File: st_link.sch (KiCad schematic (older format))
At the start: 29 parts

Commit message: STM32 schematic mostly done
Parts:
- Y?: value Crystal -> 8M
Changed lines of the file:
@@
 $Descr A4 11693 8268
 encoding utf-8
-Sheet 2 2
+Sheet 2 3
 Title "STM32 devboard with .05\" headers"
 Date ""
@@
 P 3700 2800
 AR Path="/5DFA8BC2" Ref="#PWR?"  Part="1"
-AR Path="/5DF7E971/5DFA8BC2" Ref="#PWR?"  Part="1"
-F 0 "#PWR?" H 3700 2650 50  0001 C CNN
+AR Path="/5DF7E971/5DFA8BC2" Ref="#PWR0101"  Part="1"
+F 0 "#PWR0101" H 3700 2650 50  0001 C CNN
 F 1 "+3V3" H 3715 2973 50  0000 C CNN
 F 2 "" H 3700 2800 50  0001 C CNN
@@
 P 3650 6200
 AR Path="/5DFA8BD5" Ref="#PWR?"  Part="1"
-AR Path="/5DF7E971/5DFA8BD5" Ref="#PWR?"  Part="1"
-F 0 "#PWR?" H 3650 5950 50  0001 C CNN
+AR Path="/5DF7E971/5DFA8BD5" Ref="#PWR0102"  Part="1"
+F 0 "#PWR0102" H 3650 5950 50  0001 C CNN
 F 1 "GND" H 3655 6027 50  0000 C CNN
 F 2 "" H 3650 6200 50  0001 C CNN
@@
 $EndComp
 $Comp
-L power:+3V3 #PWR?
+L power:+3V3 #PWR0103
 U 1 1 5DFA8BFA
 P 2400 2800
-F 0 "#PWR?" H 2400 2650 50  0001 C CNN
+F 0 "#PWR0103" H 2400 2650 50  0001 C CNN
 F 1 "+3V3" H 2415 2973 50  0000 C CNN
 F 2 "" H 2400 2800 50  0001 C CNN
@@
 P 2500 4000
 AR Path="/5DFA8C00" Ref="#PWR?"  Part="1"
-AR Path="/5DF7E971/5DFA8C00" Ref="#PWR?"  Part="1"
-F 0 "#PWR?" H 2500 3750 50  0001 C CNN
+AR Path="/5DF7E971/5DFA8C00" Ref="#PWR0104"  Part="1"
+F 0 "#PWR0104" H 2500 3750 50  0001 C CNN
 F 1 "GND" H 2505 3827 50  0000 C CNN
 F 2 "" H 2500 4000 50  0001 C CNN
@@
 P 1800 3900
 F 0 "Y?" H 1800 4168 50  0000 C CNN
-F 1 "Crystal" H 1800 4077 50  0000 C CNN
+F 1 "8M" H 1800 4077 50  0000 C CNN
 F 2 "" H 1800 3900 50  0001 C CNN
 F 3 "~" H 1800 3900 50  0001 C CNN
@@
 Connection ~ 2050 3900
 $Comp
-L power:GND #PWR?
+L power:GND #PWR0105
 U 1 1 5DFA8C35
 P 2050 4300
-F 0 "#PWR?" H 2050 4050 50  0001 C CNN
+F 0 "#PWR0105" H 2050 4050 50  0001 C CNN
 F 1 "GND" H 2055 4127 50  0000 C CNN
 F 2 "" H 2050 4300 50  0001 C CNN
@@
 $EndComp
 $Comp
-L power:GND #PWR?
+L power:GND #PWR0106
 U 1 1 5DFA8C3B
 P 1550 4300
-F 0 "#PWR?" H 1550 4050 50  0001 C CNN
+F 0 "#PWR0106" H 1550 4050 50  0001 C CNN
 F 1 "GND" H 1555 4127 50  0000 C CNN
 F 2 "" H 1550 4300 50  0001 C CNN
@@
 	2050 4200 2050 4300
 $Comp
-L power:GND #PWR?
+L power:GND #PWR0107
 U 1 1 5DFA8C43
 P 2900 5900
-F 0 "#PWR?" H 2900 5650 50  0001 C CNN
+F 0 "#PWR0107" H 2900 5650 50  0001 C CNN
 F 1 "GND" H 2905 5727 50  0000 C CNN
 F 2 "" H 2900 5900 50  0001 C CNN
@@
 P 5050 5750
 AR Path="/5DFA8C9C" Ref="#PWR?"  Part="1"
-AR Path="/5DF7E971/5DFA8C9C" Ref="#PWR?"  Part="1"
-F 0 "#PWR?" H 5050 5500 50  0001 C CNN
+AR Path="/5DF7E971/5DFA8C9C" Ref="#PWR0108"  Part="1"
+F 0 "#PWR0108" H 5050 5500 50  0001 C CNN
 F 1 "GND" H 5055 5577 50  0000 C CNN
 F 2 "" H 5050 5750 50  0001 C CNN
@@
 P 8550 2400
 AR Path="/5DFA8CA2" Ref="#PWR?"  Part="1"
-AR Path="/5DF7E971/5DFA8CA2" Ref="#PWR?"  Part="1"
-F 0 "#PWR?" H 8550 2250 50  0001 C CNN
+AR Path="/5DF7E971/5DFA8CA2" Ref="#PWR0109"  Part="1"
+F 0 "#PWR0109" H 8550 2250 50  0001 C CNN
 F 1 "+3V3" H 8565 2573 50  0000 C CNN
 F 2 "" H 8550 2400 50  0001 C CNN
@@
 P 9000 3150
 AR Path="/5DFA8CCF" Ref="#PWR?"  Part="1"
-AR Path="/5DF7E971/5DFA8CCF" Ref="#PWR?"  Part="1"
-F 0 "#PWR?" H 9000 2900 50  0001 C CNN
+AR Path="/5DF7E971/5DFA8CCF" Ref="#PWR0110"  Part="1"
+F 0 "#PWR0110" H 9000 2900 50  0001 C CNN
 F 1 "GND" H 9005 2977 50  0000 C CNN
 F 2 "" H 9000 3150 50  0001 C CNN
@@
 P 10150 4400
 AR Path="/5DFA8CD8" Ref="#PWR?"  Part="1"
-AR Path="/5DF7E971/5DFA8CD8" Ref="#PWR?"  Part="1"
-F 0 "#PWR?" H 10150 4150 50  0001 C CNN
+AR Path="/5DF7E971/5DFA8CD8" Ref="#PWR0111"  Part="1"
+F 0 "#PWR0111" H 10150 4150 50  0001 C CNN
 F 1 "GND" H 10155 4227 50  0000 C CNN
 F 2 "" H 10150 4400 50  0001 C CNN
@@
 P 5050 4650
 AR Path="/5DFA8CF6" Ref="#PWR?"  Part="1"
-AR Path="/5DF7E971/5DFA8CF6" Ref="#PWR?"  Part="1"
-F 0 "#PWR?" H 5050 4500 50  0001 C CNN
+AR Path="/5DF7E971/5DFA8CF6" Ref="#PWR0112"  Part="1"
+F 0 "#PWR0112" H 5050 4500 50  0001 C CNN
 F 1 "+3V3" H 5065 4823 50  0000 C CNN
 F 2 "" H 5050 4650 50  0001 C CNN
@@
 P 9300 2700
 AR Path="/5DFA8D0C" Ref="#PWR?"  Part="1"
-AR Path="/5DF7E971/5DFA8D0C" Ref="#PWR?"  Part="1"
-F 0 "#PWR?" H 9300 2550 50  0001 C CNN
+AR Path="/5DF7E971/5DFA8D0C" Ref="#PWR0113"  Part="1"
+F 0 "#PWR0113" H 9300 2550 50  0001 C CNN
 F 1 "+5V" H 9315 2873 50  0000 C CNN
 F 2 "" H 9300 2700 50  0001 C CNN
@@
 P 9350 1450
 AR Path="/5DFA8D3E" Ref="#PWR?"  Part="1"
-AR Path="/5DF7E971/5DFA8D3E" Ref="#PWR?"  Part="1"
-F 0 "#PWR?" H 9350 1300 50  0001 C CNN
+AR Path="/5DF7E971/5DFA8D3E" Ref="#PWR0114"  Part="1"
+F 0 "#PWR0114" H 9350 1300 50  0001 C CNN
 F 1 "+3V3" H 9365 1623 50  0000 C CNN
 F 2 "" H 9350 1450 50  0001 C CNN
@@
 P 9350 1850
 AR Path="/5DFA8D44" Ref="#PWR?"  Part="1"
-AR Path="/5DF7E971/5DFA8D44" Ref="#PWR?"  Part="1"
-F 0 "#PWR?" H 9350 1600 50  0001 C CNN
+AR Path="/5DF7E971/5DFA8D44" Ref="#PWR0115"  Part="1"
+F 0 "#PWR0115" H 9350 1600 50  0001 C CNN
 F 1 "GND" H 9355 1677 50  0000 C CNN
 F 2 "" H 9350 1850 50  0001 C CNN
@@
 P 2000 3300
 AR Path="/5DFA8D5B" Ref="#PWR?"  Part="1"
-AR Path="/5DF7E971/5DFA8D5B" Ref="#PWR?"  Part="1"
-F 0 "#PWR?" H 2000 3050 50  0001 C CNN
+AR Path="/5DF7E971/5DFA8D5B" Ref="#PWR0116"  Part="1"
+F 0 "#PWR0116" H 2000 3050 50  0001 C CNN
 F 1 "GND" H 2005 3127 50  0000 C CNN
 F 2 "" H 2000 3300 50  0001 C CNN
@@
 P 9650 5700
 AR Path="/5DFA8D65" Ref="#PWR?"  Part="1"
-AR Path="/5DF7E971/5DFA8D65" Ref="#PWR?"  Part="1"
-F 0 "#PWR?" H 9650 5450 50  0001 C CNN
+AR Path="/5DF7E971/5DFA8D65" Ref="#PWR0117"  Part="1"
+F 0 "#PWR0117" H 9650 5450 50  0001 C CNN
 F 1 "GND" H 9655 5527 50  0000 C CNN
 F 2 "" H 9650 5700 50  0001 C CNN
@@
 P 9650 5100
 AR Path="/5DFA8D6D" Ref="#PWR?"  Part="1"
-AR Path="/5DF7E971/5DFA8D6D" Ref="#PWR?"  Part="1"
-F 0 "#PWR?" H 9650 4950 50  0001 C CNN
+AR Path="/5DF7E971/5DFA8D6D" Ref="#PWR0118"  Part="1"
+F 0 "#PWR0118" H 9650 4950 50  0001 C CNN
 F 1 "+3V3" H 9665 5273 50  0000 C CNN
 F 2 "" H 9650 5100 50  0001 C CNN
@@
 P 6250 2700
 AR Path="/5DFA8DB0" Ref="#PWR?"  Part="1"
-AR Path="/5DF7E971/5DFA8DB0" Ref="#PWR?"  Part="1"
-F 0 "#PWR?" H 6250 2450 50  0001 C CNN
+AR Path="/5DF7E971/5DFA8DB0" Ref="#PWR0119"  Part="1"
+F 0 "#PWR0119" H 6250 2450 50  0001 C CNN
 F 1 "GND" H 6255 2527 50  0000 C CNN
 F 2 "" H 6250 2700 50  0001 C CNN
@@
 P 7050 2000
 AR Path="/5DFA8DBB" Ref="#PWR?"  Part="1"
-AR Path="/5DF7E971/5DFA8DBB" Ref="#PWR?"  Part="1"
-F 0 "#PWR?" H 7050 1850 50  0001 C CNN
+AR Path="/5DF7E971/5DFA8DBB" Ref="#PWR0120"  Part="1"
+F 0 "#PWR0120" H 7050 1850 50  0001 C CNN
 F 1 "+3V3" H 7065 2173 50  0000 C CNN
 F 2 "" H 7050 2000 50  0001 C CNN
@@
 P 5450 2000
 AR Path="/5DFA8DC1" Ref="#PWR?"  Part="1"
-AR Path="/5DF7E971/5DFA8DC1" Ref="#PWR?"  Part="1"
-F 0 "#PWR?" H 5450 1850 50  0001 C CNN
+AR Path="/5DF7E971/5DFA8DC1" Ref="#PWR0121"  Part="1"
+F 0 "#PWR0121" H 5450 1850 50  0001 C CNN
 F 1 "+5V" H 5465 2173 50  0000 C CNN
 F 2 "" H 5450 2000 50  0001 C CNN

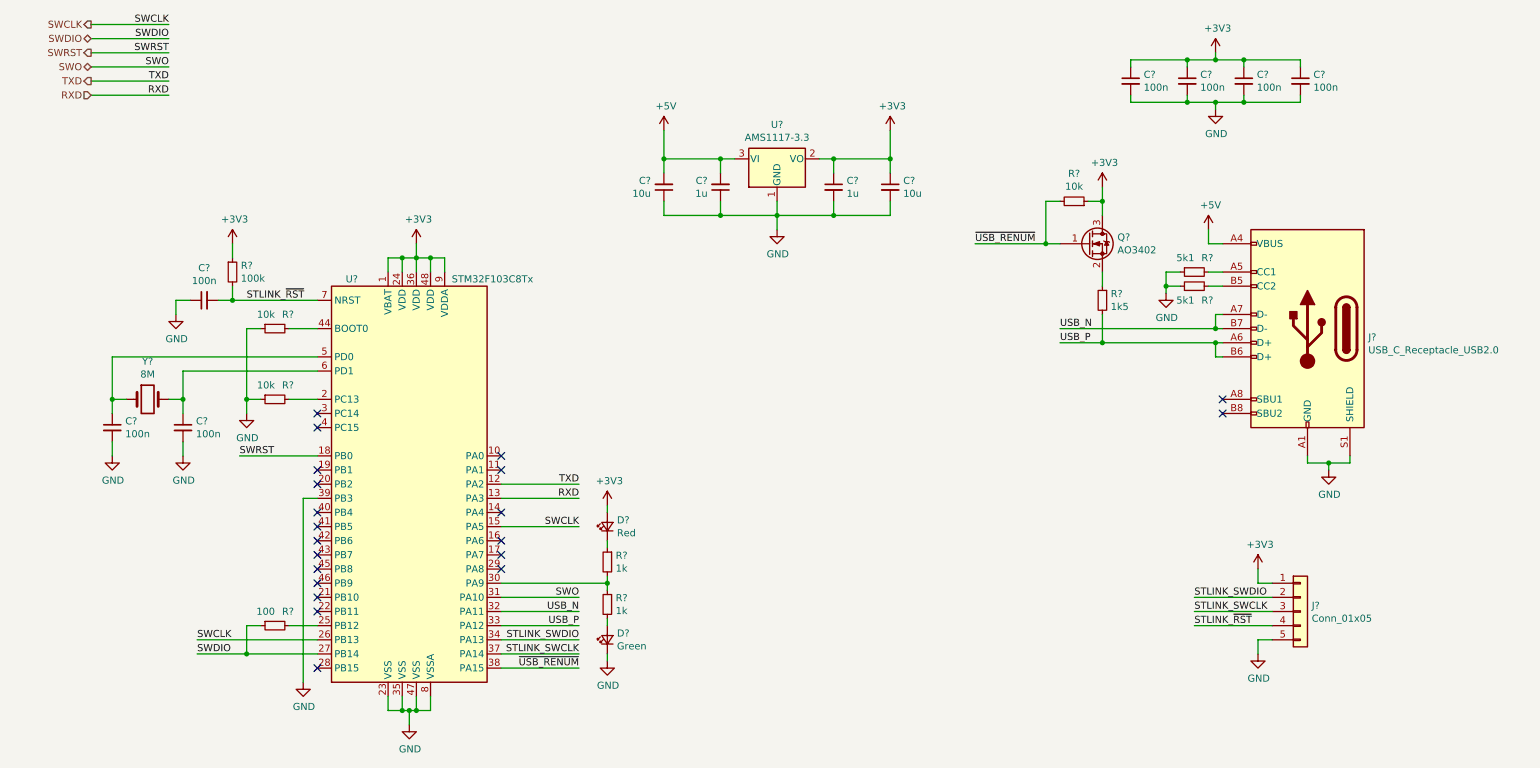
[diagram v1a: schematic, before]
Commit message: Better sch segmentation and add TCA6424A symbol
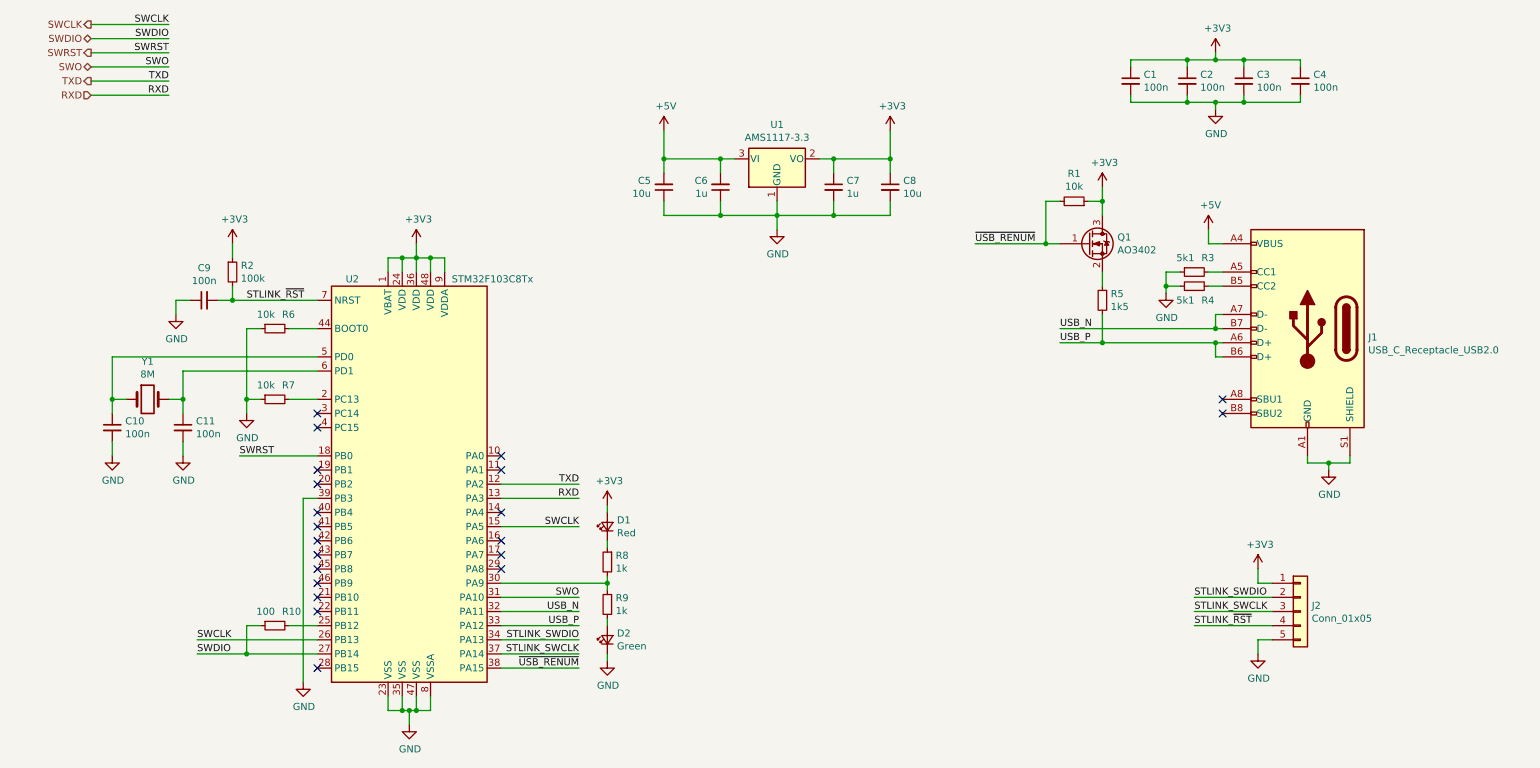
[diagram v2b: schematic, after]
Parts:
- C1, C10, C11, C2, C3, C4, C5, C6, C7, C8, C9: renamed from C?; footprint (none) -> Capacitor_SMD:C_0603_1608Metric
- D1, D2: renamed from D?; footprint (none) -> LED_SMD:LED_0603_1608Metric
- J1: renamed from J?; footprint (none) -> Connector_USB:USB_C_Receptacle_Palconn_UTC16-G
- J2: renamed from J?; footprint (none) -> Connector_PinHeader_2.54mm:PinHeader_1x05_P2.54mm_Vertical
- R1, R10, R2, R3, R4, R5, R6, R7, R8, R9: renamed from R?; footprint (none) -> Resistor_SMD:R_0603_1608Metric
- Y1: renamed from Y?; footprint (none) -> Crystal:Crystal_HC52-U_Vertical
- gave numbers to parts that had none: 3

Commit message: Schematic mostly done, place begun
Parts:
- Y1: footprint Crystal:Crystal_HC52-U_Vertical -> Crystal:Crystal_HC18-U_Vertical
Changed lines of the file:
@@
 F 0 "Y1" H 1800 4168 50  0000 C CNN
 F 1 "8M" H 1800 4077 50  0000 C CNN
-F 2 "Crystal:Crystal_HC52-U_Vertical" H 1800 3900 50  0001 C CNN
+F 2 "Crystal:Crystal_HC18-U_Vertical" H 1800 3900 50  0001 C CNN
 F 3 "~" H 1800 3900 50  0001 C CNN
 	1    1800 3900

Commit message: Routing should be done
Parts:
- J1: footprint Connector_USB:USB_C_Receptacle_Palconn_UTC16-G -> antboard:USB_C_Receptacle_Palconn_UTC16-G
- Y1: footprint Crystal:Crystal_HC18-U_Vertical -> Crystal:Crystal_HC49-4H_Vertical
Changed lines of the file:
@@
 F 0 "Y1" H 1800 4168 50  0000 C CNN
 F 1 "8M" H 1800 4077 50  0000 C CNN
-F 2 "Crystal:Crystal_HC18-U_Vertical" H 1800 3900 50  0001 C CNN
+F 2 "Crystal:Crystal_HC49-4H_Vertical" H 1800 3900 50  0001 C CNN
 F 3 "~" H 1800 3900 50  0001 C CNN
 	1    1800 3900
@@
 F 0 "J1" H 9570 3339 50  0000 R CNN
 F 1 "USB_C_Receptacle_USB2.0" H 9570 3248 50  0000 R CNN
-F 2 "Connector_USB:USB_C_Receptacle_Palconn_UTC16-G" H 10150 3400 50  0001 C CNN
+F 2 "antboard:USB_C_Receptacle_Palconn_UTC16-G" H 10150 3400 50  0001 C CNN
 F 3 "https://www.usb.org/sites/default/files/documents/usb_type-c.zip" H 10150 3400 50  0001 C CNN
 	1    10000 3400
